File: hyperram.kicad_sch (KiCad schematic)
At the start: 7 parts, among them U11 S27KL0641DABHI023

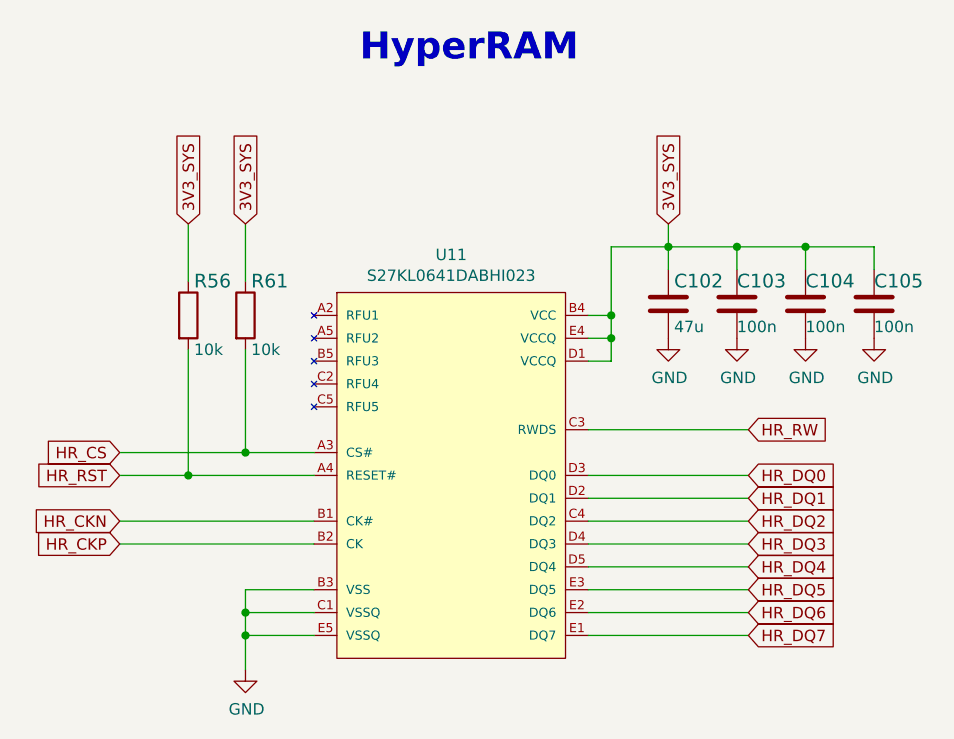
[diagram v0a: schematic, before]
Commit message: Placement and routing of FT4232H. Re annotation of the schematics
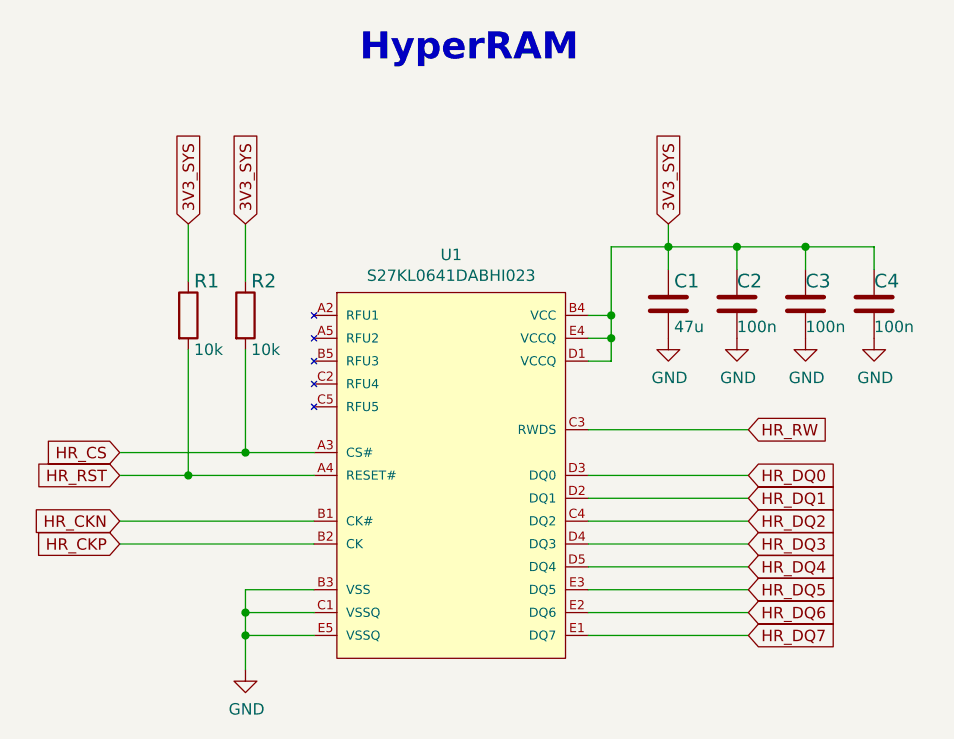
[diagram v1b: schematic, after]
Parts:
- renumbered C102 to C1, C103 to C2, C104 to C3, C105 to C4, R56 to R1, R61 to R2, U11 to U1
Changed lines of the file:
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@@
   (symbol (lib_id "lpddr4-test-board:S27KL0641DABHI023") (at 96.52 110.49 0) (unit 1)
     (in_bom yes) (on_board yes)
-    (property "Reference" "U11" (id 0) (at 96.52 85.979 0))
+    (property "Reference" "U1" (id 0) (at 96.52 85.979 0))
     (property "Value" "S27KL0641DABHI023" (id 1) (at 96.52 88.2904 0))
     (property "Footprint" "lpddr4-test-board-footprints:FBGA-24" (id 2) (at 85.09 138.43 0)
@@
   (symbol (lib_id "lpddr4-test-board:C_47u_0603") (at 120.65 91.44 0) (unit 1)
     (in_bom yes) (on_board yes)
-    (property "Reference" "C102" (id 0) (at 121.285 88.9 0)
+    (property "Reference" "C1" (id 0) (at 121.285 88.9 0)
       (effects (font (size 1.524 1.524)) (justify left))
     )
@@
   (symbol (lib_id "lpddr4-test-board:C_100n_0402_6V3") (at 135.89 91.44 0) (unit 1)
     (in_bom yes) (on_board yes)
-    (property "Reference" "C104" (id 0) (at 135.89 88.9 0)
+    (property "Reference" "C3" (id 0) (at 135.89 88.9 0)
       (effects (font (size 1.524 1.524)) (justify left))
     )
@@
   (symbol (lib_id "lpddr4-test-board:GND") (at 120.65 95.25 0) (unit 1)
     (in_bom yes) (on_board yes)
-    (property "Reference" "#PWR0260" (id 0) (at 120.65 101.6 0)
+    (property "Reference" "#PWR02" (id 0) (at 120.65 101.6 0)
       (effects (font (size 1.27 1.27)) hide)
     )
@@
   (symbol (lib_id "lpddr4-test-board:R_10k_0402") (at 67.31 92.71 270) (unit 1)
     (in_bom yes) (on_board yes)
-    (property "Reference" "R56" (id 0) (at 67.945 88.9 90)
+    (property "Reference" "R1" (id 0) (at 67.945 88.9 90)
       (effects (font (size 1.524 1.524)) (justify left))
     )
@@
   (symbol (lib_id "lpddr4-test-board:GND") (at 128.27 95.25 0) (unit 1)
     (in_bom yes) (on_board yes)
-    (property "Reference" "#PWR0261" (id 0) (at 128.27 101.6 0)
+    (property "Reference" "#PWR03" (id 0) (at 128.27 101.6 0)
       (effects (font (size 1.27 1.27)) hide)
     )
@@
   (symbol (lib_id "lpddr4-test-board:GND") (at 135.89 95.25 0) (unit 1)
     (in_bom yes) (on_board yes)
-    (property "Reference" "#PWR0262" (id 0) (at 135.89 101.6 0)
+    (property "Reference" "#PWR04" (id 0) (at 135.89 101.6 0)
       (effects (font (size 1.27 1.27)) hide)
     )
@@
   (symbol (lib_id "lpddr4-test-board:C_100n_0402_6V3") (at 128.27 91.44 0) (unit 1)
     (in_bom yes) (on_board yes)
-    (property "Reference" "C103" (id 0) (at 128.27 88.9 0)
+    (property "Reference" "C2" (id 0) (at 128.27 88.9 0)
       (effects (font (size 1.524 1.524)) (justify left))
     )
@@
   (symbol (lib_id "lpddr4-test-board:R_10k_0402") (at 73.66 92.71 270) (unit 1)
     (in_bom yes) (on_board yes)
-    (property "Reference" "R61" (id 0) (at 74.295 88.9 90)
+    (property "Reference" "R2" (id 0) (at 74.295 88.9 90)
       (effects (font (size 1.524 1.524)) (justify left))
     )
@@
   (symbol (lib_id "lpddr4-test-board:GND") (at 73.66 132.08 0) (unit 1)
     (in_bom yes) (on_board yes)
-    (property "Reference" "#PWR0263" (id 0) (at 73.66 138.43 0)
+    (property "Reference" "#PWR01" (id 0) (at 73.66 138.43 0)
       (effects (font (size 1.27 1.27)) hide)
     )
@@
   (symbol (lib_id "lpddr4-test-board:C_100n_0402_6V3") (at 143.51 91.44 0) (unit 1)
     (in_bom yes) (on_board yes)
-    (property "Reference" "C105" (id 0) (at 143.51 88.9 0)
+    (property "Reference" "C4" (id 0) (at 143.51 88.9 0)
       (effects (font (size 1.524 1.524)) (justify left))
     )
@@
   (symbol (lib_id "lpddr4-test-board:GND") (at 143.51 95.25 0) (unit 1)
     (in_bom yes) (on_board yes)
-    (property "Reference" "#PWR0264" (id 0) (at 143.51 101.6 0)
-      (effects (font (size 1.27 1.27)) hide)
-    )
+    (property "Reference" "#PWR05" (id 0) (at 143.51 101.6 0)
+      (effects (font (size 1.27 1.27)) hide)
+    )
